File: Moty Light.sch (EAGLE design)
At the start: 16 parts, among them Q1 C1815, Q2 C1815

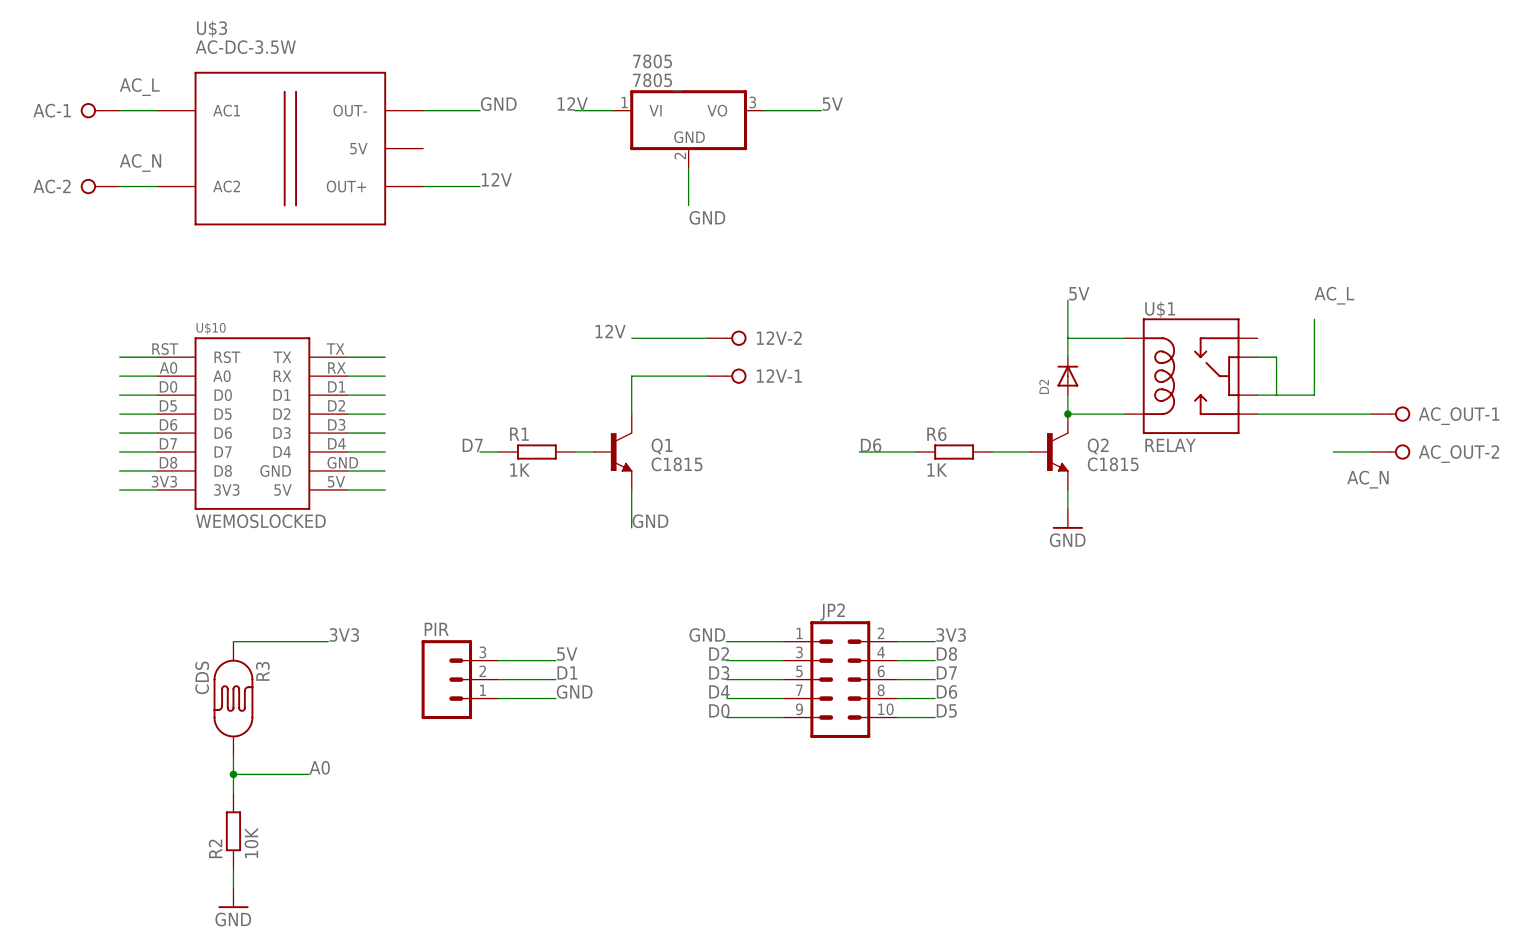
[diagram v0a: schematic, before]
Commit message: Update to new version to match size of new box
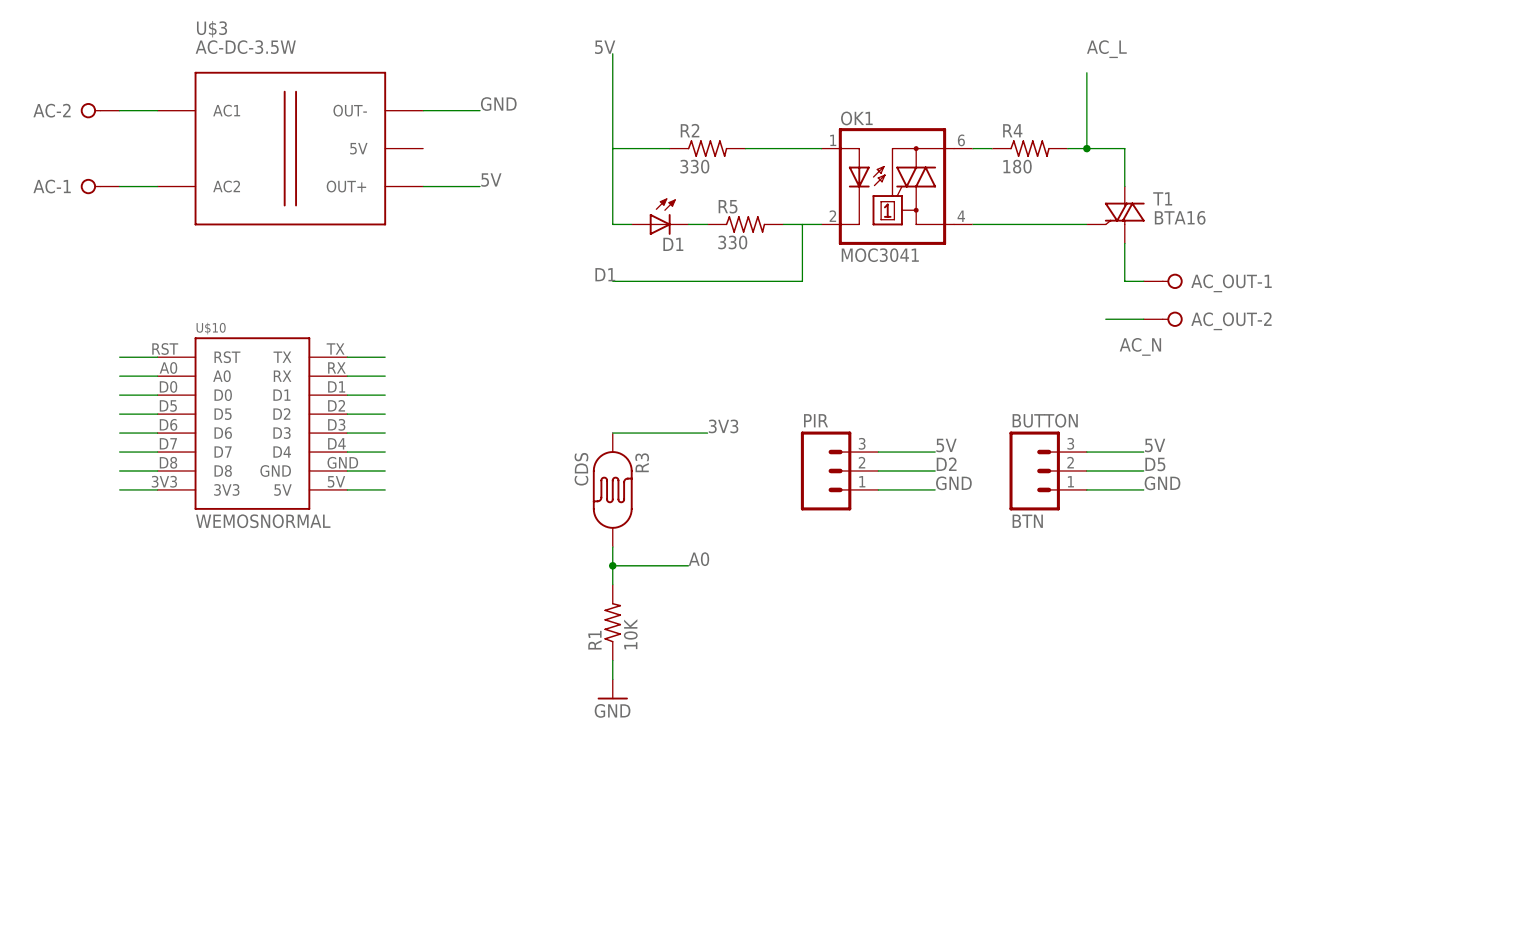
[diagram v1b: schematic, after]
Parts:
- removed 12V: (no value), con-wago-508:W237-02P
- removed 7805: 7805_, linear:7805TV
- removed D2: (no value), adafruit:DIODESMA
- removed JP2: (no value), SparkFun-Connectors:M05X2PTH
- removed Q1, Q2: C1815, SparkFun-DiscreteSemi:TRANSISTOR_NPNMMBT2222A
- removed R6: 1K, rcl:R-EU_R0805
- removed U$1: RELAY, My Eagle Lib:MINIATURE_RELAY_JRC_21F
- added BUTTON: BTN, SparkFun-Connectors:M03PTH
- added D1: (no value), led:LED3MM
- added OK1: MOC3041, optocoupler:MOC3032T
- added R4: 180, rcl:R-US_0204/7
- added R5: 330, rcl:R-US_0204/7
- added T1: BTA16, triac:BT138-V
- R1: value 1K -> 10K; device rcl:R-EU_R0805 -> rcl:R-US_0204/7
- R2: value 10K -> 330; device rcl:R-EU_R0805 -> rcl:R-US_0204/7
- U$10: value WEMOSLOCKED -> WEMOSNORMAL; device My Eagle Lib:WEMOSLOCKED -> My Eagle Lib:WEMOSNORMAL
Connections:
- removed net 12V: 12V-2.KL, 7805.VI, U$3.OUT+
- removed net N$1: 12V-1.KL, Q1.C
- removed net N$3: D2.A, Q2.C, U$1.COIL2
- removed net N$4: Q2.B, R6.2
- removed net N$7: Q1.B, R1.2
- removed net N$8: AC_OUT-1.KL, U$1.NO
- new net N$10: OK1.A, R2.2
- new net N$14: OK1.A2, R4.1
- new net N$23: AC_OUT-1.KL, T1.A1
- new net N$28: D1.C, R5.1
- new net N$9: OK1.A1, T1.G
- net 3V3: no longer JP2.2
- net 5V: now also BUTTON.3, D1.A, R2.1, U$3.OUT+; no longer 7805.VO, D2.C, U$1.COIL1
- net A0: now also R1.2; no longer R2.2
- net AC_L: now also AC-2.KL, R4.2, T1.A2; no longer AC-1.KL, U$1.COM1, U$1.COM2
- net AC_N: now also AC-1.KL; no longer AC-2.KL
- net D0: no longer JP2.9
- net D1: now also OK1.C, R5.2; no longer PIR.2
- net D2: now also PIR.2; no longer JP2.3
- net D3: no longer JP2.5
- net D4: no longer JP2.7
- net D5: now also BUTTON.2; no longer JP2.10
- net D6: no longer JP2.8, R6.1
- net D7: no longer JP2.6, R1.1
- net D8: no longer JP2.4
- net GND: now also BUTTON.1, R1.1; no longer 7805.GND, JP2.1, Q1.E, Q2.E, R2.1
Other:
- moved on the sheet: AC-1, AC-2, AC_OUT-1, AC_OUT-2, PIR, R3

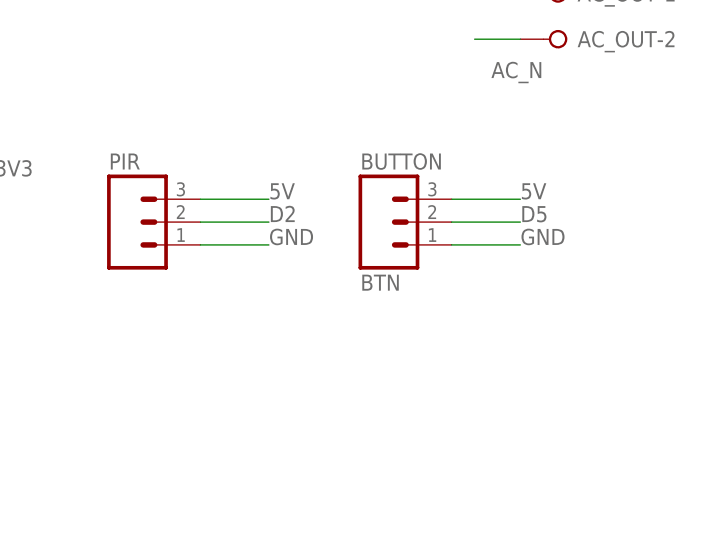
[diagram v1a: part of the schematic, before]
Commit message: Update design to use SSR and fit in a box and update code to support view status and config via web
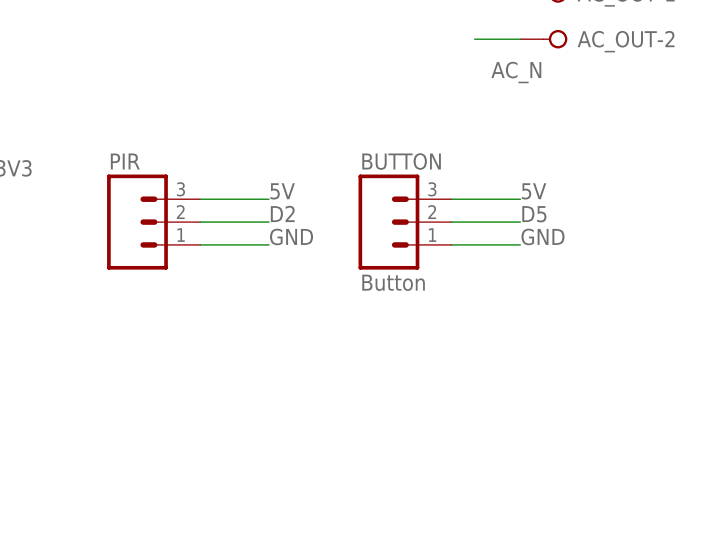
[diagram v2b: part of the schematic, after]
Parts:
- BUTTON: value BTN -> Button
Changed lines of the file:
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@@
 <grid distance="0.1" unitdist="inch" unit="inch" style="lines" multiple="1" display="no" altdistance="0.01" altunitdist="inch" altunit="inch"/>
 <layers>
-<layer number="1" name="Top" color="4" fill="1" visible="yes" active="no"/>
-<layer number="16" name="Bottom" color="1" fill="1" visible="yes" active="no"/>
-<layer number="17" name="Pads" color="2" fill="1" visible="yes" active="no"/>
-<layer number="18" name="Vias" color="2" fill="1" visible="yes" active="no"/>
-<layer number="19" name="Unrouted" color="6" fill="1" visible="yes" active="no"/>
-<layer number="20" name="Dimension" color="15" fill="1" visible="yes" active="no"/>
-<layer number="21" name="tPlace" color="7" fill="1" visible="yes" active="no"/>
-<layer number="22" name="bPlace" color="7" fill="1" visible="yes" active="no"/>
-<layer number="23" name="tOrigins" color="15" fill="1" visible="yes" active="no"/>
-<layer number="24" name="bOrigins" color="15" fill="1" visible="yes" active="no"/>
-<layer number="25" name="tNames" color="7" fill="1" visible="yes" active="no"/>
-<layer number="26" name="bNames" color="7" fill="1" visible="yes" active="no"/>
-<layer number="27" name="tValues" color="7" fill="1" visible="yes" active="no"/>
-<layer number="28" name="bValues" color="7" fill="1" visible="yes" active="no"/>
+<layer number="1" name="Top" color="4" fill="1" visible="no" active="no"/>
+<layer number="16" name="Bottom" color="1" fill="1" visible="no" active="no"/>
+<layer number="17" name="Pads" color="2" fill="1" visible="no" active="no"/>
+<layer number="18" name="Vias" color="2" fill="1" visible="no" active="no"/>
+<layer number="19" name="Unrouted" color="6" fill="1" visible="no" active="no"/>
+<layer number="20" name="Dimension" color="15" fill="1" visible="no" active="no"/>
+<layer number="21" name="tPlace" color="7" fill="1" visible="no" active="no"/>
+<layer number="22" name="bPlace" color="7" fill="1" visible="no" active="no"/>
+<layer number="23" name="tOrigins" color="15" fill="1" visible="no" active="no"/>
+<layer number="24" name="bOrigins" color="15" fill="1" visible="no" active="no"/>
+<layer number="25" name="tNames" color="7" fill="1" visible="no" active="no"/>
+<layer number="26" name="bNames" color="7" fill="1" visible="no" active="no"/>
+<layer number="27" name="tValues" color="7" fill="1" visible="no" active="no"/>
+<layer number="28" name="bValues" color="7" fill="1" visible="no" active="no"/>
 <layer number="29" name="tStop" color="7" fill="3" visible="no" active="no"/>
 <layer number="30" name="bStop" color="7" fill="6" visible="no" active="no"/>
@@
 <layer number="35" name="tGlue" color="7" fill="4" visible="no" active="no"/>
 <layer number="36" name="bGlue" color="7" fill="5" visible="no" active="no"/>
-<layer number="37" name="tTest" color="7" fill="1" visible="yes" active="no"/>
-<layer number="38" name="bTest" color="7" fill="1" visible="yes" active="no"/>
+<layer number="37" name="tTest" color="7" fill="1" visible="no" active="no"/>
+<layer number="38" name="bTest" color="7" fill="1" visible="no" active="no"/>
 <layer number="39" name="tKeepout" color="4" fill="11" visible="no" active="no"/>
 <layer number="40" name="bKeepout" color="1" fill="11" visible="no" active="no"/>
@@
 <layer number="44" name="Drills" color="7" fill="1" visible="no" active="no"/>
 <layer number="45" name="Holes" color="7" fill="1" visible="no" active="no"/>
-<layer number="46" name="Milling" color="3" fill="1" visible="yes" active="no"/>
-<layer number="47" name="Measures" color="7" fill="1" visible="yes" active="no"/>
-<layer number="48" name="Document" color="7" fill="1" visible="yes" active="no"/>
-<layer number="49" name="Reference" color="7" fill="1" visible="yes" active="no"/>
-<layer number="50" name="dxf" color="7" fill="1" visible="yes" active="no"/>
-<layer number="51" name="tDocu" color="7" fill="1" visible="yes" active="no"/>
-<layer number="52" name="bDocu" color="7" fill="1" visible="yes" active="no"/>
-<layer number="53" name="tGND_GNDA" color="7" fill="1" visible="yes" active="no"/>
-<layer number="54" name="bGND_GNDA" color="7" fill="1" visible="yes" active="no"/>
-<layer number="56" name="wert" color="7" fill="1" visible="yes" active="no"/>
-<layer number="57" name="tCAD" color="7" fill="1" visible="yes" active="no"/>
-<layer number="59" name="tCarbon" color="7" fill="1" visible="yes" active="no"/>
-<layer number="60" name="bCarbon" color="7" fill="1" visible="yes" active="no"/>
+<layer number="46" name="Milling" color="3" fill="1" visible="no" active="no"/>
+<layer number="47" name="Measures" color="7" fill="1" visible="no" active="no"/>
+<layer number="48" name="Document" color="7" fill="1" visible="no" active="no"/>
+<layer number="49" name="Reference" color="7" fill="1" visible="no" active="no"/>
+<layer number="50" name="dxf" color="7" fill="1" visible="no" active="no"/>
+<layer number="51" name="tDocu" color="7" fill="1" visible="no" active="no"/>
+<layer number="52" name="bDocu" color="7" fill="1" visible="no" active="no"/>
+<layer number="53" name="tGND_GNDA" color="7" fill="1" visible="no" active="no"/>
+<layer number="54" name="bGND_GNDA" color="7" fill="1" visible="no" active="no"/>
+<layer number="56" name="wert" color="7" fill="1" visible="no" active="no"/>
+<layer number="57" name="tCAD" color="7" fill="1" visible="no" active="no"/>
+<layer number="59" name="tCarbon" color="7" fill="1" visible="no" active="no"/>
+<layer number="60" name="bCarbon" color="7" fill="1" visible="no" active="no"/>
 <layer number="90" name="Modules" color="5" fill="1" visible="yes" active="yes"/>
 <layer number="91" name="Nets" color="2" fill="1" visible="yes" active="yes"/>
@@
 <part name="R5" library="rcl" deviceset="R-US_" device="0204/7" value="330"/>
 <part name="T1" library="triac" deviceset="BT138" device="-V" value="BTA16"/>
-<part name="BUTTON" library="SparkFun-Connectors" deviceset="M03" device="PTH" value="BTN"/>
+<part name="BUTTON" library="SparkFun-Connectors" deviceset="M03" device="PTH" value="Button"/>
 </parts>
 <sheets>

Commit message: Update to version 0.2
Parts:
- removed AC_OUT: (no value), con-wago-508:W237-02P
- removed BUTTON: Button, SparkFun-Connectors:M03PTH
- removed OK1: MOC3041, optocoupler:MOC3032T
- removed T1: BTA16, triac:BT138-V
- added AC1, AC2: (no value), con-wago-508:W237-02P
- added BTN2: BTN2, SparkFun-Connectors:M03PTH
- added BUTTON1: BTN1, SparkFun-Connectors:M03PTH
- added C1, C1815: C1815, SparkFun-DiscreteSemi:TRANSISTOR_NPNSOT23-3
- added C2: 47uF/16V, SparkFun-Capacitors:CAP_POLPTH2
- added C3: 102pF, SparkFun-Capacitors:CAP_POLPTH2
- added D2: (no value), adafruit:DIODESMA
- added N1: N4148, adafruit:DIODESOD-123
- added N4148: (no value), adafruit:DIODESOD-123
- added PWR_LED: PWR, adafruit:LED3MM
- added R6, R8, R9: 1K, rcl:R-EU_R0805
- added R7: 4.7K, rcl:R-EU_R0805
- added RELAY1, RELAY2: ZNS5106, relay:ZNS5106
- added RELAY_LED1: RELAY1, adafruit:LED3MM
- added RELAY_LED2: Relay2, adafruit:LED3MM
- D1: device led:LED3MM -> adafruit:DIODESMA
- R1: device rcl:R-US_0204/7 -> rcl:R-US_R0805
- R2, R5: value 330 -> 1K; device rcl:R-US_0204/7 -> rcl:R-EU_R0805
- R4: value 180 -> 4.7K; device rcl:R-US_0204/7 -> rcl:R-EU_R0805
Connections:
- removed net AC_L: AC-2.KL, R4.2, T1.A2, U$3.AC1
- removed net AC_N: AC-1.KL, AC_OUT-2.KL, U$3.AC2
- removed net N$14: OK1.A2, R4.1
- removed net N$23: AC_OUT-1.KL, T1.A1
- removed net N$28: D1.C, R5.1
- new net HOT: AC-2.KL, RELAY12.P, RELAY22.P, U$3.AC1
- new net N$1: C1815.C, D2.A, RELAY11.2, RELAY_LED1.C
- new net N$3: N4148.C, R6.1
- new net N$4: R8.2, RELAY_LED1.A
- new net N$5: C1.C, D1.A, RELAY21.2, RELAY_LED2.C
- new net N$6: C1.B, R2.2, R4.2
- new net N$7: C1815.B, R6.2, R7.2
- new net N$8: N1.C, R2.1
- new net NC1: RELAY12.O
- new net NC2: RELAY22.O
- new net NEUTRAL: AC-1.KL, AC1-2.KL, AC2-2.KL, U$3.AC2
- new net NO1: AC1-1.KL, RELAY12.S
- new net NO2: AC2-1.KL, RELAY22.S
- net 5V: now also BTN2.3, BUTTON1.3, C2.+, C3.+, D1.C, D2.C, R5.1, R8.1, R9.1, RELAY11.1, RELAY21.1; no longer BUTTON.3, D1.A, R2.1
- net D1: now also N4148.A; no longer OK1.C, R5.2
- net D2: now also N1.A; no longer PIR.2
- net D5: now also BUTTON1.2; no longer BUTTON.2
- net D6: now also BTN2.2
- net D7: now also PIR.2
- net GND: now also BTN2.1, BUTTON1.1, C1.E, C1815.E, C2.-, C3.-, PWR_LED.C, R4.1, R7.1; no longer BUTTON.1
- net N$10: now also PWR_LED.A, R9.2; no longer OK1.A, R2.2
- net N$9: now also R5.2, RELAY_LED2.A; no longer OK1.A1, T1.G
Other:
- note added: "2016-10-06 http://easytech.vn"
- note added: "Moty Light V0.2"
- note added: "Power & Wemos D1 Mini"
- note added: "Relays"
- note added: "Sensors & Controls"
- moved on the sheet: PIR, R1, R3, U$10

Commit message: Update design to version 0.3
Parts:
- removed C1, C1815: C1815, SparkFun-DiscreteSemi:TRANSISTOR_NPNSOT23-3
- added Q1, Q2: C1815, SparkFun-DiscreteSemi:TRANSISTOR_NPNSOT23-3
- RELAY_LED1: value RELAY1 -> Relay1
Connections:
- net GND: now also Q1.E, Q2.E; no longer C1.E, C1815.E
- net N$1: now also Q1.C; no longer C1815.C
- net N$5: now also Q2.C; no longer C1.C
- net N$6: now also Q2.B; no longer C1.B
- net N$7: now also Q1.B; no longer C1815.B
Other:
- note added: "2016-10-19 http://easytech.vn"
- note added: "Moty Light V0.3"
- note removed: "2016-10-06 http://easytech.vn"
- note removed: "Moty Light V0.2"
- moved on the sheet: AC1-1, AC1-2, AC2-1, AC2-2, D1, D2, N1, N4148, PWR_LED, R2, R4, R5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

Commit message: Update design to version 1.0
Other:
- note added: "Moty Light v1.0"
- note removed: "Moty Light V0.3"
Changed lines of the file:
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@@
 <wire x1="317.5" y1="50.8" x2="83.82" y2="50.8" width="0.1524" layer="97"/>
 <wire x1="83.82" y1="50.8" x2="83.82" y2="104.14" width="0.1524" layer="97"/>
-<text x="236.22" y="162.56" size="6.35" layer="97" font="vector" ratio="15">Moty Light V0.3</text>
+<text x="236.22" y="162.56" size="6.35" layer="97" font="vector" ratio="15">Moty Light v1.0</text>
 <text x="236.22" y="144.78" size="5.08" layer="97" font="vector" ratio="15">2016-10-19
 http://easytech.vn</text>
